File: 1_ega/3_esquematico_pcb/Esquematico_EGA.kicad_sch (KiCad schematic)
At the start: 66 parts, among them J1 ±5V, J2 UART, J3 Encoder, J4 CP2102, J5 OUT, J6 IN, J7 DDS, J8 Conn_01x14, J9 Conn_01x14, Q1 2N7000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

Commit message: actualización PCB y esquemático
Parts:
- TP7: value Vin -> DDS_out
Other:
- moved on the sheet: TP7
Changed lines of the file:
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@@
 	(wire
 		(pts
-			(xy 158.75 144.78) (xy 167.64 144.78)
+			(xy 157.48 144.78) (xy 166.37 144.78)
 		)
 		(stroke
@@
 	)
 	(label "DDS_OUT"
-		(at 158.75 144.78 0)
+		(at 157.48 144.78 0)
 		(effects
 			(font
@@
 	(symbol
 		(lib_id "Connector:TestPoint")
-		(at 167.64 144.78 270)
+		(at 166.37 144.78 270)
 		(unit 1)
 		(body_style 1)
@@
 		(fields_autoplaced yes)
 		(property "Reference" "TP7"
-			(at 172.72 143.5099 90)
+			(at 171.45 143.5099 90)
 			(show_name no)
 			(do_not_autoplace no)
@@
 			)
 		)
-		(property "Value" "Vin"
-			(at 172.72 146.0499 90)
+		(property "Value" "DDS_out"
+			(at 171.45 146.0499 90)
 			(show_name no)
 			(do_not_autoplace no)
@@
 		)
 		(property "Footprint" "Connector_PinHeader_2.54mm:PinHeader_1x01_P2.54mm_Vertical"
-			(at 167.64 149.86 0)
+			(at 166.37 149.86 0)
 			(hide yes)
 			(show_name no)
@@
 		)
 		(property "Datasheet" ""
-			(at 167.64 149.86 0)
+			(at 166.37 149.86 0)
 			(hide yes)
 			(show_name no)
@@
 		)
 		(property "Description" "test point"
-			(at 167.64 144.78 0)
+			(at 166.37 144.78 0)
 			(hide yes)
 			(show_name no)

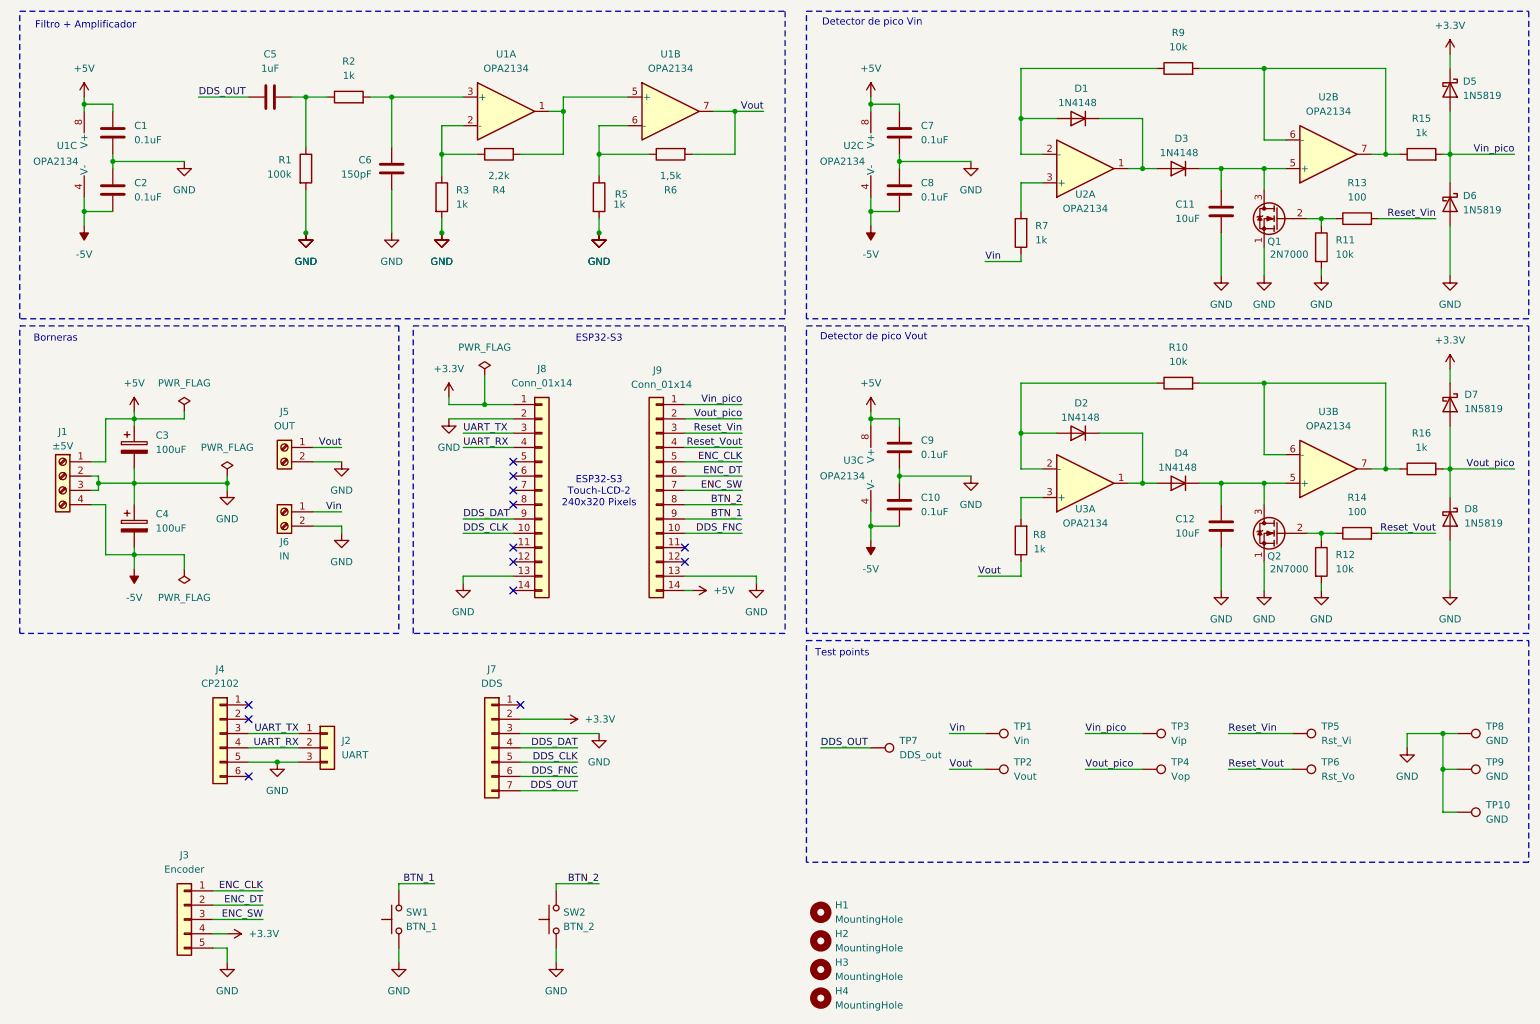
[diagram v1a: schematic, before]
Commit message: Cambiar operacional por el TL072
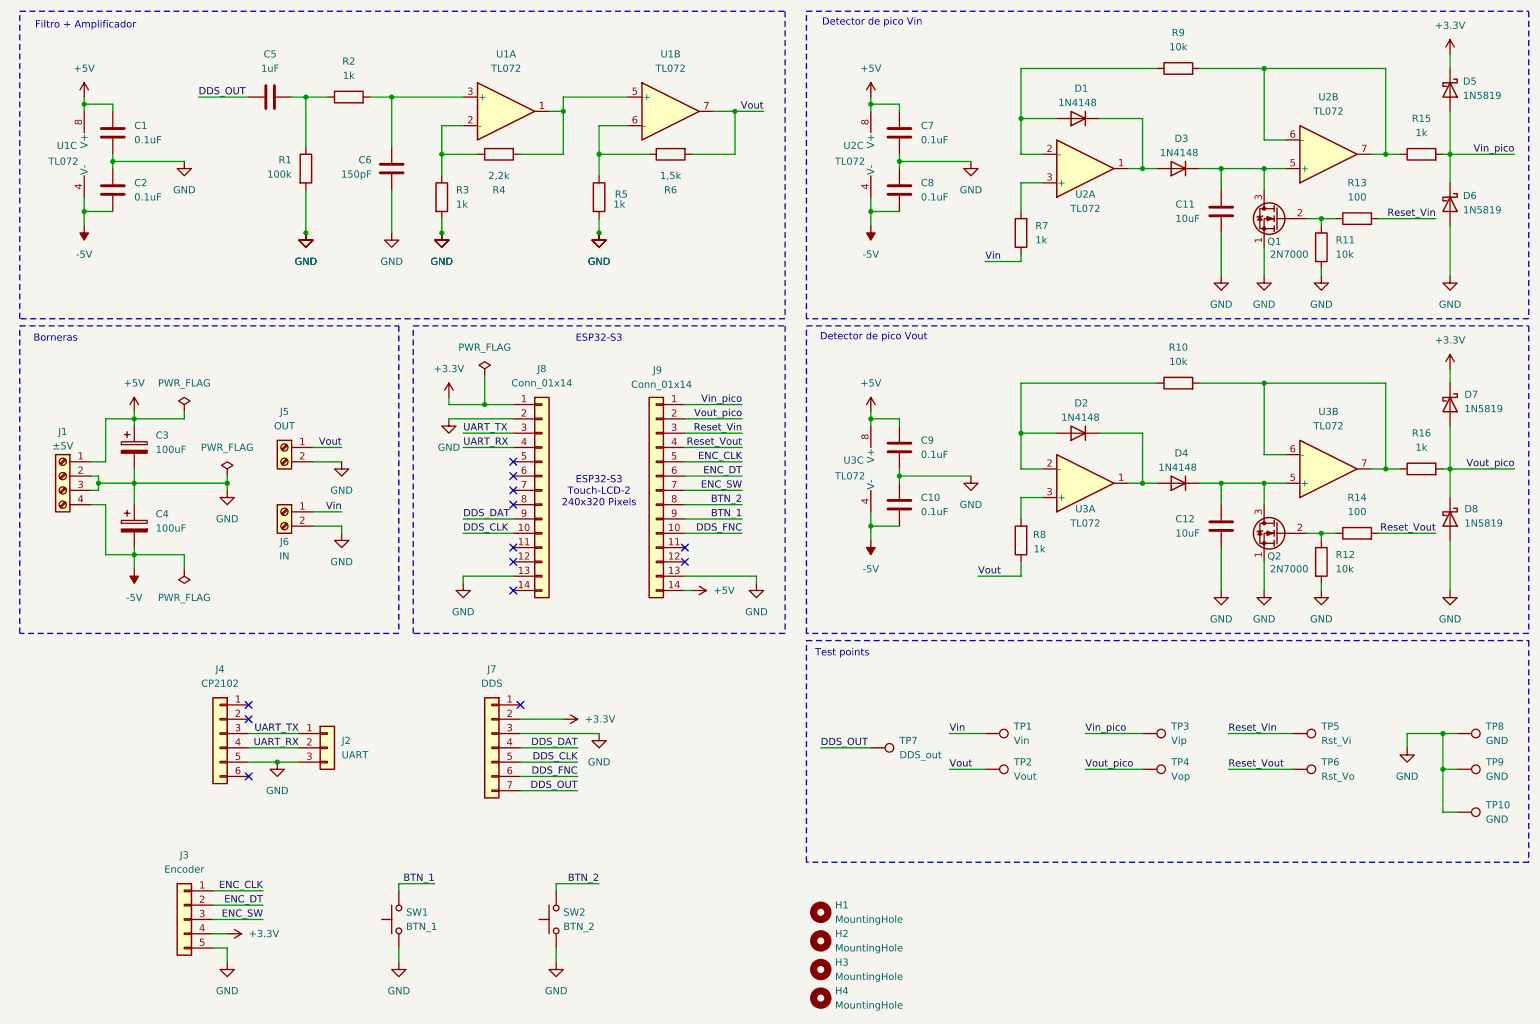
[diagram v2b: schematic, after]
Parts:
- U1, U2, U3: value OPA2134 -> TL072
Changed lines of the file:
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@@
 			)
 		)
-		(property "Value" "OPA2134"
+		(property "Value" "TL072"
 			(at 25.654 40.64 0)
 			(show_name no)
@@
 			)
 		)
-		(property "Value" "OPA2134"
+		(property "Value" "TL072"
 			(at 101.6 24.13 0)
 			(show_name no)
@@
 			)
 		)
-		(property "Value" "OPA2134"
+		(property "Value" "TL072"
 			(at 130.81 24.13 0)
 			(show_name no)
@@
 			)
 		)
-		(property "Value" "OPA2134"
+		(property "Value" "TL072"
 			(at 247.65 87.63 0)
 			(show_name no)
@@
 			)
 		)
-		(property "Value" "OPA2134"
+		(property "Value" "TL072"
 			(at 247.65 31.75 0)
 			(show_name no)
@@
 			)
 		)
-		(property "Value" "OPA2134"
+		(property "Value" "TL072"
 			(at 165.354 96.52 0)
 			(show_name no)
@@
 			)
 		)
-		(property "Value" "OPA2134"
+		(property "Value" "TL072"
 			(at 204.47 104.902 0)
 			(show_name no)
@@
 			)
 		)
-		(property "Value" "OPA2134"
+		(property "Value" "TL072"
 			(at 204.47 49.022 0)
 			(show_name no)
@@
 			)
 		)
-		(property "Value" "OPA2134"
+		(property "Value" "TL072"
 			(at 165.354 40.64 0)
 			(show_name no)

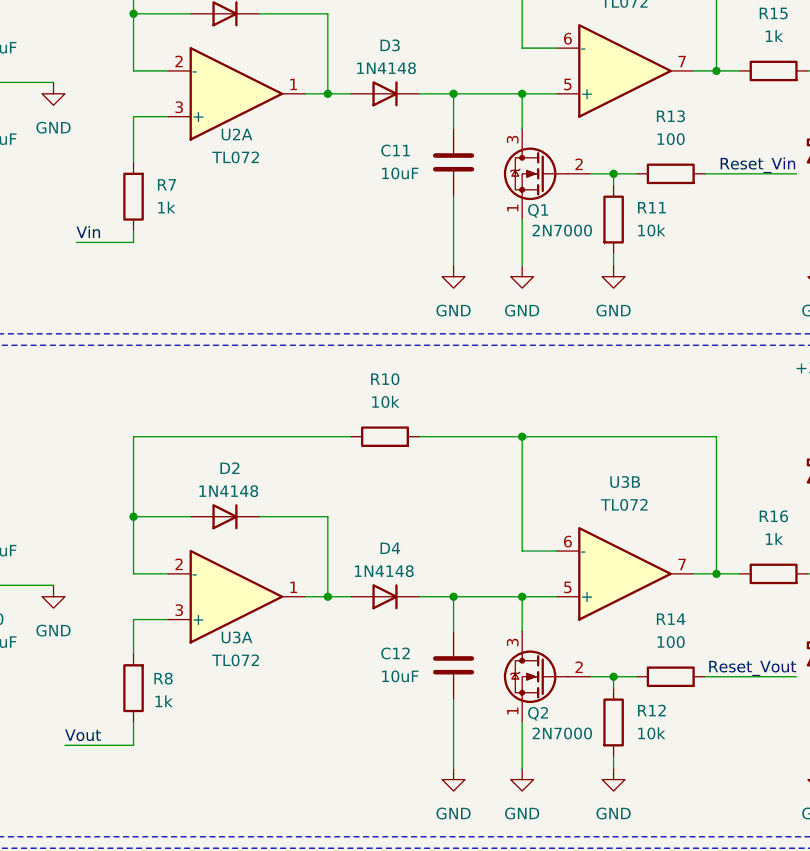
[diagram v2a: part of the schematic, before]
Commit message: docs: actualizar valores de componentes
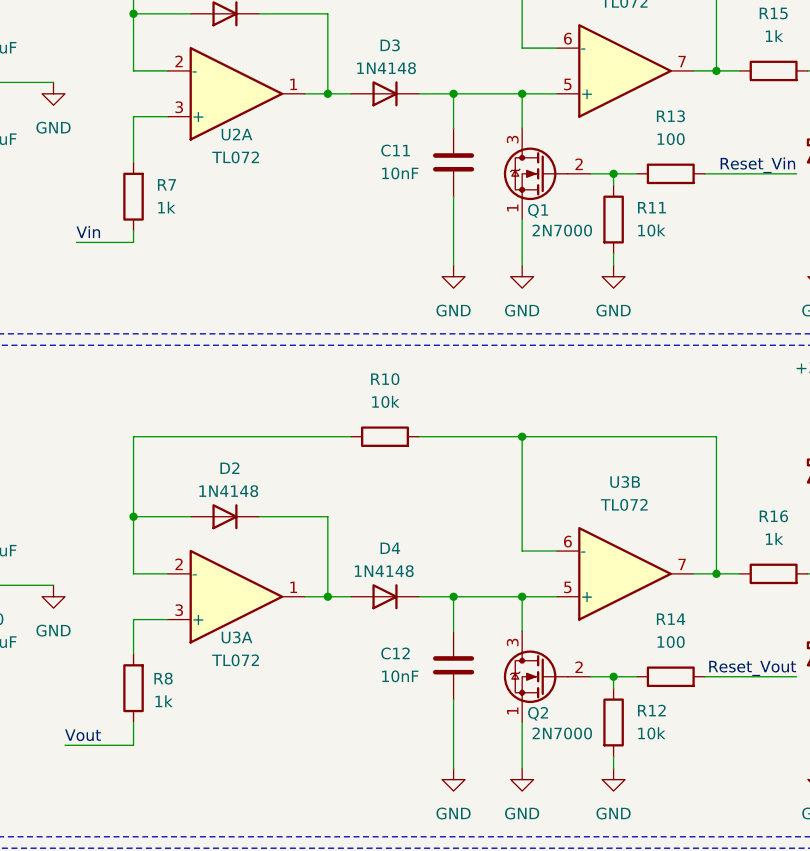
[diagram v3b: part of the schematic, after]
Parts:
- C11, C12: value 10uF -> 10nF
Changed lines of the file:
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@@
 			)
 		)
-		(property "Value" "10uF"
+		(property "Value" "10nF"
 			(at 220.472 50.8 0)
 			(show_name no)
@@
 			)
 		)
-		(property "Value" "10uF"
+		(property "Value" "10nF"
 			(at 220.472 106.68 0)
 			(show_name no)
